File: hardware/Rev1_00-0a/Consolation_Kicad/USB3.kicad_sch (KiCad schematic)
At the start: 12 parts, among them J1 0484050003, U3 AP2192AFGEG-7

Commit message: Work on block diagram and top-level schematic sheet Work on PinMux
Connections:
- net RP2350_USB_VBUS: no longer names the net of U3.6 (OUT2)
- no-connect marks 0 -> 1
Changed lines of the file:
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@@
 		(color 0 0 0 0)
+	)
+	(no_connect
+		(at 194.945 86.36)
 	)
 	(bus_entry
@@
 		(pts
 			(xy 138.43 105.41) (xy 236.855 105.41)
-		)
-		(stroke
-			(width 0)
-			(type default)
-		)
-	)
-	(wire
-		(pts
-			(xy 194.945 86.36) (xy 203.835 86.36)
 		)
 		(stroke
@@
 		)
 	)
-	(hierarchical_label "RP2350_USB_VBUS"
-		(shape output)
-		(at 203.835 86.36 0)
-		(effects
-			(font
-				(size 1.27 1.27)
-			)
-			(justify left)
-		)
-	)

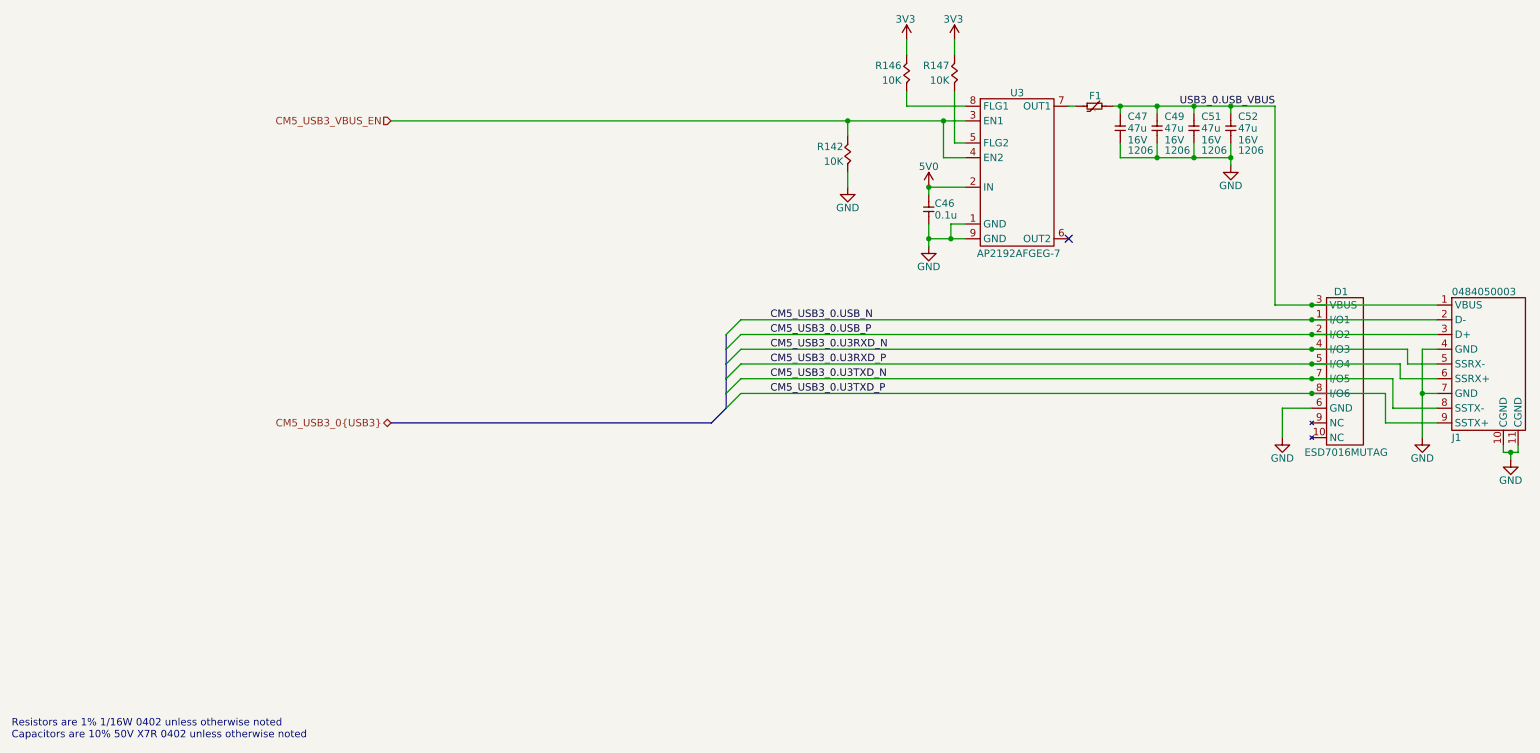
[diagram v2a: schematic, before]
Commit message: Removed unnecessary functions (USB2 mux, CapTouch) Adjusted 220uF alum capacitor for codec (slimmer version)
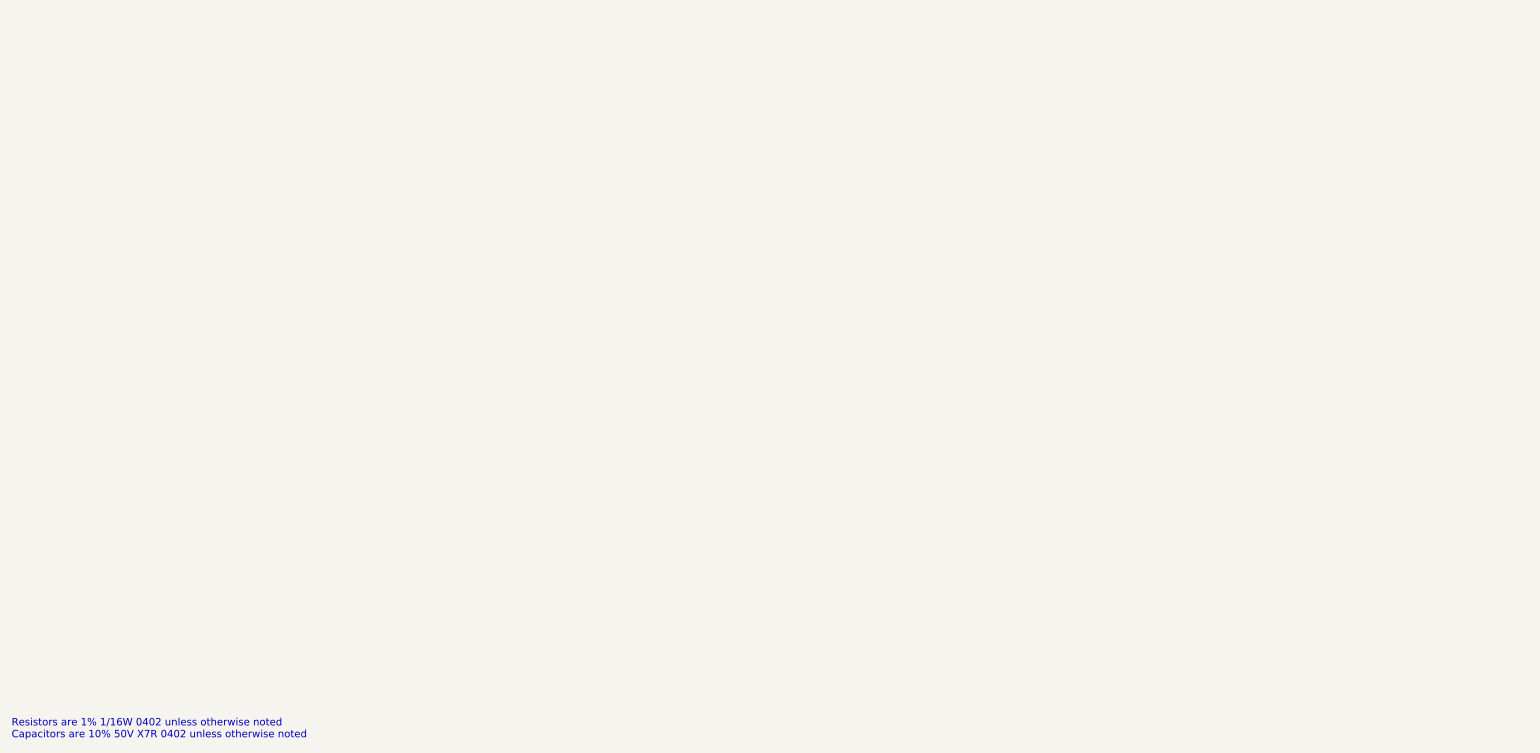
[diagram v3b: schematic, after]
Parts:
- removed C46: 0.1u, footprint:CAP_NONPOL_0402, symbol KicadCompDb:Capacitors/CAP_CER_SMT_00001
- removed C47, C49, C51, C52: 47u, footprint:CAP_NONPOL_1206, symbol KicadCompDb:Capacitors/CAP_CER_SMT_00010
- removed D1: ESD7016MUTAG, footprint:UDFN8, symbol KicadCompDb:ESD Diodes/ESD_DIODE_00001
- removed F1: MINISMDC050F-2, footprint:PTC_1812, symbol KicadCompDb:PTC Resettable fuse/PTC_00001
- removed J1: 0484050003, footprint:0484050003, symbol KicadCompDb:Connector/CONN_00009
- removed R142, R146, R147: 10K, footprint:RES_0402, symbol KicadCompDb:Resistors/RES_SMT_00013
- removed U3: AP2192AFGEG-7, footprint:U-DFN3030-8, symbol KicadCompDb:Load Switch/LOAD_SW_00002
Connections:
- no-connect marks 1 -> 0
